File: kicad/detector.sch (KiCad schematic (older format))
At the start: 41 parts, among them J1 Conn_01x05_Male, J2 Conn_01x05_Male, U1 LT1761-5, U2 LT1964-5, U3 REF5010ID, U4 OPA2197xD, U5 OPA2197xD

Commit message: move detector power supplies around (wip)
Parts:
- added H?: MountingHole_Pad, symbol Mechanical:MountingHole_Pad
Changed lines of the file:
@@
 Text Label 10100 1250 0    50   ~ 0
 -Y1
+$Comp
+L Mechanical:MountingHole_Pad H?
+U 1 1 5EA4D075
+P 10100 3450
+F 0 "H?" H 10200 3499 50  0000 L CNN
+F 1 "MountingHole_Pad" H 10200 3408 50  0000 L CNN
+F 2 "" H 10100 3450 50  0001 C CNN
+F 3 "~" H 10100 3450 50  0001 C CNN
+	1    10100 3450
+	1    0    0    -1
+$EndComp
 $EndSCHEMATC

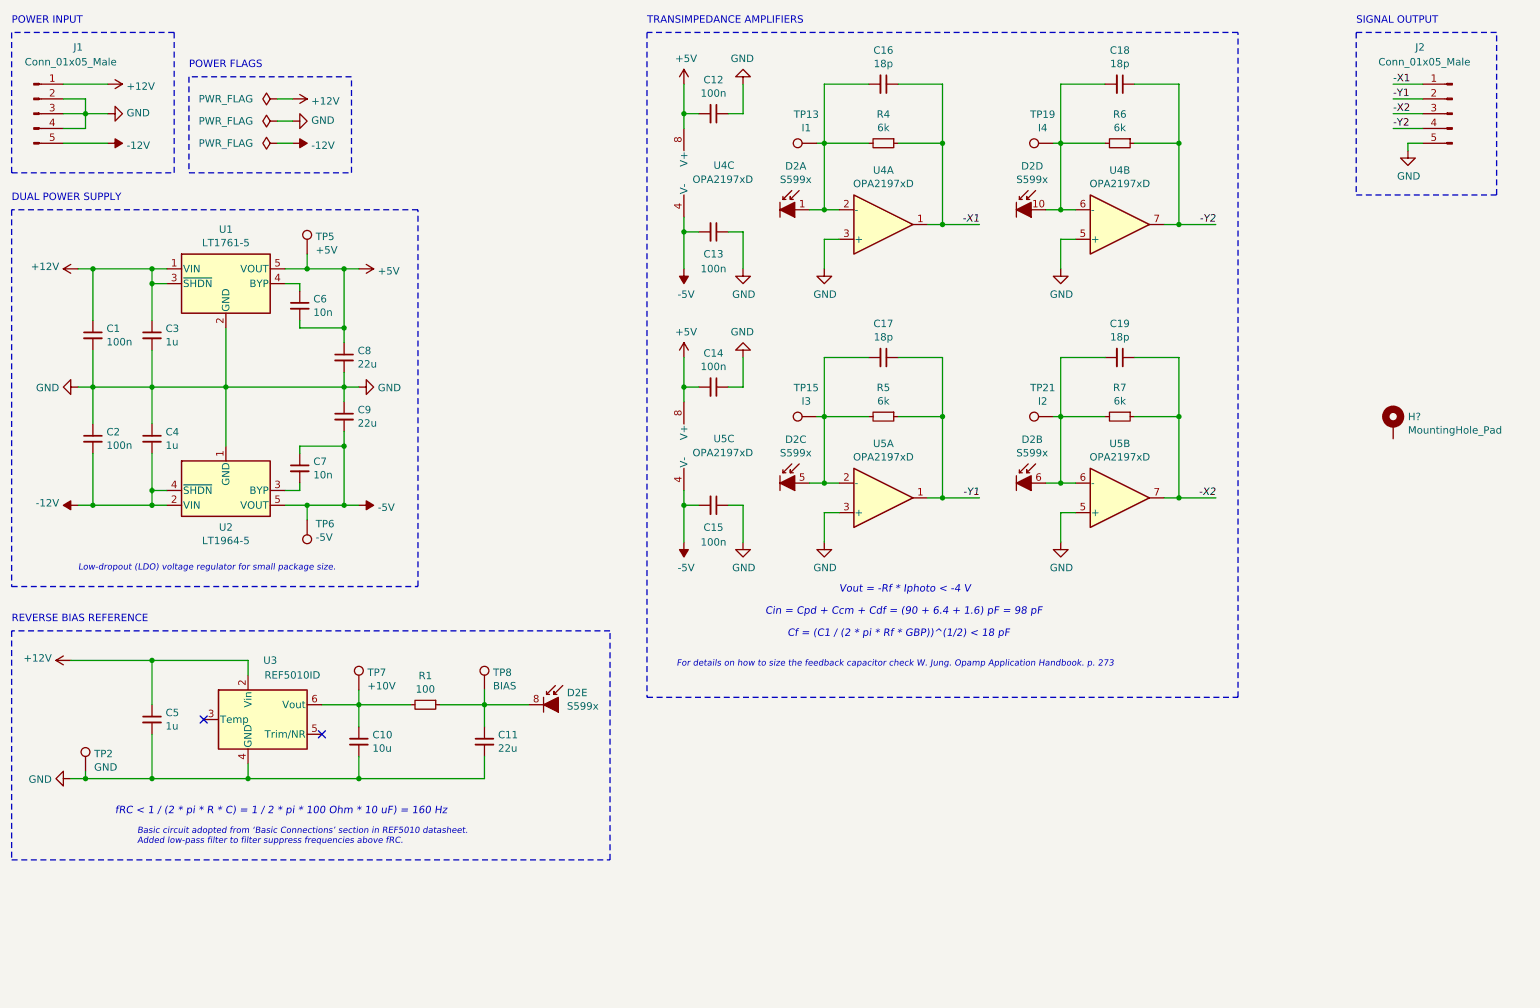
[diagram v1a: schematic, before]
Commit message: added mounting holes to eeschema, replaced mounting holes with pad
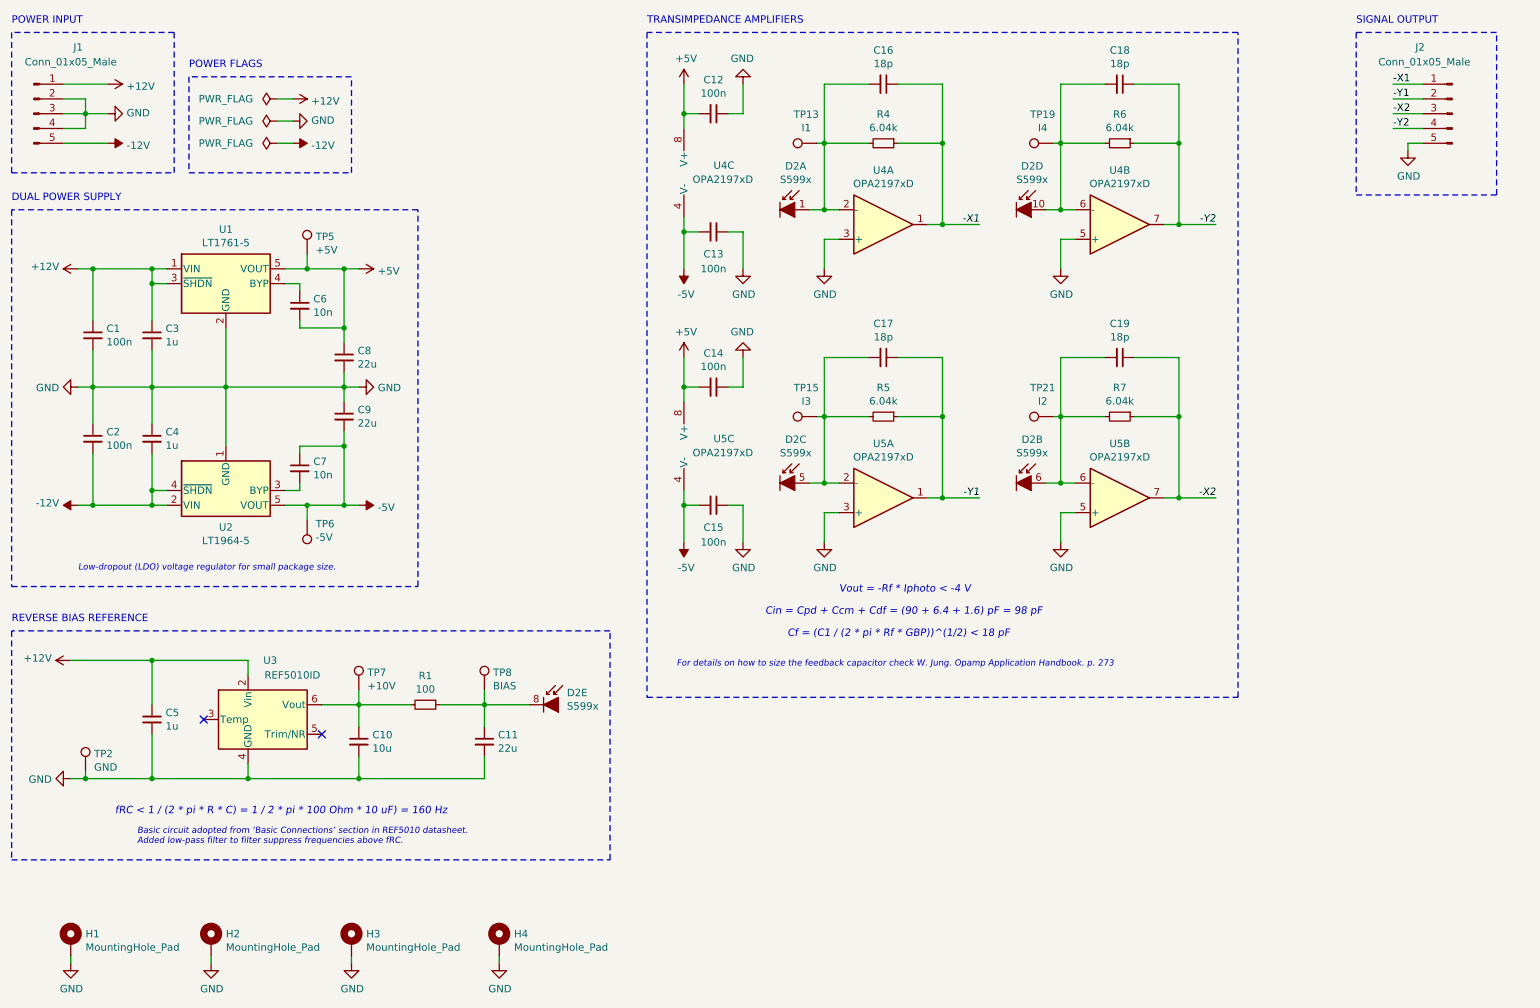
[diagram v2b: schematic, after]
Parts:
- removed H?: MountingHole_Pad, symbol Mechanical:MountingHole_Pad
- added H1, H2, H3, H4: MountingHole_Pad, MountingHole:MountingHole_2.7mm_M2.5_Pad, symbol Mechanical:MountingHole_Pad
- R4, R5, R6, R7: value 6k -> 6.04k
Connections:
- net GND: now also H1.1, H2.1, H3.1, H4.1
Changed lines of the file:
@@
 P 8250 1550
 F 0 "R6" V 8054 1550 50  0000 C CNN
-F 1 "6k" V 8145 1550 50  0000 C CNN
+F 1 "6.04k" V 8145 1550 50  0000 C CNN
 F 2 "Resistor_SMD:R_0603_1608Metric" H 8250 1550 50  0001 C CNN
 F 3 "~" H 8250 1550 50  0001 C CNN
@@
 P 6650 1550
 F 0 "R4" V 6454 1550 50  0000 C CNN
-F 1 "6k" V 6545 1550 50  0000 C CNN
+F 1 "6.04k" V 6545 1550 50  0000 C CNN
 F 2 "Resistor_SMD:R_0603_1608Metric" H 6650 1550 50  0001 C CNN
 F 3 "~" H 6650 1550 50  0001 C CNN
@@
 P 8250 3400
 F 0 "R7" V 8054 3400 50  0000 C CNN
-F 1 "6k" V 8145 3400 50  0000 C CNN
+F 1 "6.04k" V 8145 3400 50  0000 C CNN
 F 2 "Resistor_SMD:R_0603_1608Metric" H 8250 3400 50  0001 C CNN
 F 3 "~" H 8250 3400 50  0001 C CNN
@@
 P 6650 3400
 F 0 "R5" V 6454 3400 50  0000 C CNN
-F 1 "6k" V 6545 3400 50  0000 C CNN
+F 1 "6.04k" V 6545 3400 50  0000 C CNN
 F 2 "Resistor_SMD:R_0603_1608Metric" H 6650 3400 50  0001 C CNN
 F 3 "~" H 6650 3400 50  0001 C CNN
@@
 -Y1
 $Comp
-L Mechanical:MountingHole_Pad H?
-U 1 1 5EA4D075
-P 10100 3450
-F 0 "H?" H 10200 3499 50  0000 L CNN
-F 1 "MountingHole_Pad" H 10200 3408 50  0000 L CNN
-F 2 "" H 10100 3450 50  0001 C CNN
-F 3 "~" H 10100 3450 50  0001 C CNN
-	1    10100 3450
-	1    0    0    -1
-$EndComp
+L Mechanical:MountingHole_Pad H1
+U 1 1 5EA3A96B
+P 1150 6950
+F 0 "H1" H 1250 6999 50  0000 L CNN
+F 1 "MountingHole_Pad" H 1250 6908 50  0000 L CNN
+F 2 "MountingHole:MountingHole_2.7mm_M2.5_Pad" H 1150 6950 50  0001 C CNN
+F 3 "~" H 1150 6950 50  0001 C CNN
+	1    1150 6950
+	1    0    0    -1
+$EndComp
+$Comp
+L Mechanical:MountingHole_Pad H2
+U 1 1 5EA3B177
+P 2100 6950
+F 0 "H2" H 2200 6999 50  0000 L CNN
+F 1 "MountingHole_Pad" H 2200 6908 50  0000 L CNN
+F 2 "MountingHole:MountingHole_2.7mm_M2.5_Pad" H 2100 6950 50  0001 C CNN
+F 3 "~" H 2100 6950 50  0001 C CNN
+	1    2100 6950
+	1    0    0    -1
+$EndComp
+$Comp
+L Mechanical:MountingHole_Pad H3
+U 1 1 5EA3BD34
+P 3050 6950
+F 0 "H3" H 3150 6999 50  0000 L CNN
+F 1 "MountingHole_Pad" H 3150 6908 50  0000 L CNN
+F 2 "MountingHole:MountingHole_2.7mm_M2.5_Pad" H 3050 6950 50  0001 C CNN
+F 3 "~" H 3050 6950 50  0001 C CNN
+	1    3050 6950
+	1    0    0    -1
+$EndComp
+$Comp
+L Mechanical:MountingHole_Pad H4
+U 1 1 5EA3BF9A
+P 4050 6950
+F 0 "H4" H 4150 6999 50  0000 L CNN
+F 1 "MountingHole_Pad" H 4150 6908 50  0000 L CNN
+F 2 "MountingHole:MountingHole_2.7mm_M2.5_Pad" H 4050 6950 50  0001 C CNN
+F 3 "~" H 4050 6950 50  0001 C CNN
+	1    4050 6950
+	1    0    0    -1
+$EndComp
+$Comp
+L power:GND #PWR0115
+U 1 1 5EA3CCB1
+P 1150 7100
+F 0 "#PWR0115" H 1150 6850 50  0001 C CNN
+F 1 "GND" H 1155 6927 50  0000 C CNN
+F 2 "" H 1150 7100 50  0001 C CNN
+F 3 "" H 1150 7100 50  0001 C CNN
+	1    1150 7100
+	1    0    0    -1
+$EndComp
+Wire Wire Line
+	1150 7100 1150 7050
+$Comp
+L power:GND #PWR0116
+U 1 1 5EA46D11
+P 2100 7100
+F 0 "#PWR0116" H 2100 6850 50  0001 C CNN
+F 1 "GND" H 2105 6927 50  0000 C CNN
+F 2 "" H 2100 7100 50  0001 C CNN
+F 3 "" H 2100 7100 50  0001 C CNN
+	1    2100 7100
+	1    0    0    -1
+$EndComp
+Wire Wire Line
+	2100 7100 2100 7050
+$Comp
+L power:GND #PWR0117
+U 1 1 5EA50D8F
+P 3050 7100
+F 0 "#PWR0117" H 3050 6850 50  0001 C CNN
+F 1 "GND" H 3055 6927 50  0000 C CNN
+F 2 "" H 3050 7100 50  0001 C CNN
+F 3 "" H 3050 7100 50  0001 C CNN
+	1    3050 7100
+	1    0    0    -1
+$EndComp
+Wire Wire Line
+	3050 7100 3050 7050
+$Comp
+L power:GND #PWR0118
+U 1 1 5EA64F10
+P 4050 7100
+F 0 "#PWR0118" H 4050 6850 50  0001 C CNN
+F 1 "GND" H 4055 6927 50  0000 C CNN
+F 2 "" H 4050 7100 50  0001 C CNN
+F 3 "" H 4050 7100 50  0001 C CNN
+	1    4050 7100
+	1    0    0    -1
+$EndComp
+Wire Wire Line
+	4050 7100 4050 7050
 $EndSCHEMATC

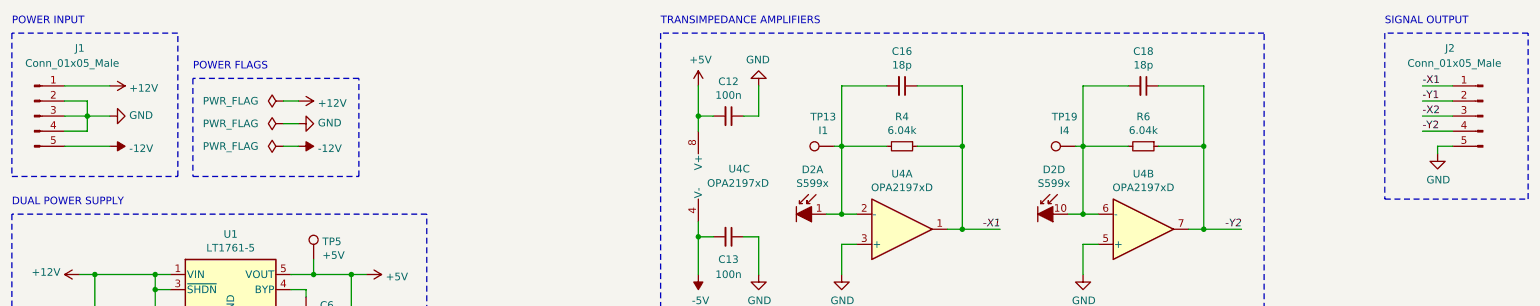
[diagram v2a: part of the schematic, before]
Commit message: changed header shield pins for improved detector routing
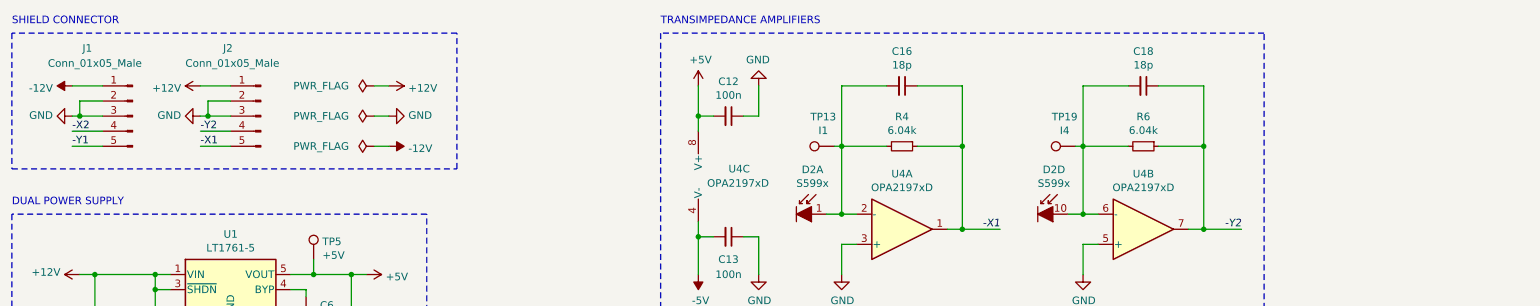
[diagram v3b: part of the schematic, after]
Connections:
- net +12V: now also J2.1 (Pin_1); no longer J1.1 (Pin_1)
- net -12V: now also J1.1 (Pin_1); no longer J1.5 (Pin_5)
- net -X1: now also J2.5 (Pin_5); no longer J2.1 (Pin_1)
- net -X2: now also J1.4 (Pin_4); no longer J2.3 (Pin_3)
- net -Y1: now also J1.5 (Pin_5); no longer J2.2 (Pin_2)
- net GND: now also J2.2 (Pin_2), J2.3 (Pin_3); no longer J1.4 (Pin_4), J2.5 (Pin_5)
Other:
- note added: "SHIELD CONNECTOR"
- note removed: "POWER FLAGS"
- note removed: "POWER INPUT"
- note removed: "SIGNAL OUTPUT"
- moved on the sheet: J1, J2
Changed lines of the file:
@@
 	1    0    0    1
 $EndComp
-Text Label 10100 1150 0    50   ~ 0
+Text Label 2000 1550 0    50   ~ 0
 -X1
-Wire Wire Line
-	10100 1150 10300 1150
-Text Label 10100 1350 0    50   ~ 0
+Text Label 1150 1450 0    50   ~ 0
 -X2
 Wire Wire Line
-	10100 1250 10300 1250
-Wire Wire Line
-	10100 1350 10300 1350
-Wire Wire Line
-	10100 1450 10300 1450
-Wire Notes Line
-	750  800  750  1750
-Wire Notes Line
-	1850 1750 1850 800
-Wire Notes Line
-	1850 800  750  800
-Text Notes 750  750  0    50   ~ 0
-POWER INPUT
-Wire Notes Line
-	9850 1900 10800 1900
-Wire Notes Line
-	10800 1900 10800 800
-Wire Notes Line
-	10800 800  9850 800
-Wire Notes Line
-	9850 800  9850 1900
-Text Notes 9850 750  0    50   ~ 0
-SIGNAL OUTPUT
+	2050 1250 2200 1250
+Wire Wire Line
+	2050 1350 2200 1350
+Wire Wire Line
+	2000 1450 2200 1450
 Wire Wire Line
 	6250 2200 6250 2400
@@
 L power:PWR_FLAG #FLG0103
 U 1 1 5E844871
-P 2550 1250
-F 0 "#FLG0103" H 2550 1325 50  0001 C CNN
-F 1 "PWR_FLAG" V 2550 1600 50  0000 C CNN
-F 2 "" H 2550 1250 50  0001 C CNN
-F 3 "~" H 2550 1250 50  0001 C CNN
-	1    2550 1250
+P 3150 1150
+F 0 "#FLG0103" H 3150 1225 50  0001 C CNN
+F 1 "PWR_FLAG" V 3150 1500 50  0000 C CNN
+F 2 "" H 3150 1150 50  0001 C CNN
+F 3 "~" H 3150 1150 50  0001 C CNN
+	1    3150 1150
 	0    -1   1    0
 $EndComp
@@
 L power:+12V #PWR0101
 U 1 1 5EB34081
-P 2650 1250
-F 0 "#PWR0101" H 2650 1100 50  0001 C CNN
-F 1 "+12V" V 2665 1378 50  0000 L CNN
-F 2 "" H 2650 1250 50  0001 C CNN
-F 3 "" H 2650 1250 50  0001 C CNN
-	1    2650 1250
+P 3250 1150
+F 0 "#PWR0101" H 3250 1000 50  0001 C CNN
+F 1 "+12V" V 3265 1278 50  0000 L CNN
+F 2 "" H 3250 1150 50  0001 C CNN
+F 3 "" H 3250 1150 50  0001 C CNN
+	1    3250 1150
 	0    1    1    0
 $EndComp
@@
 L power:GND #PWR0102
 U 1 1 5EB6A7CA
-P 2650 1400
-F 0 "#PWR0102" H 2650 1150 50  0001 C CNN
-F 1 "GND" V 2655 1272 50  0000 R CNN
-F 2 "" H 2650 1400 50  0001 C CNN
-F 3 "" H 2650 1400 50  0001 C CNN
-	1    2650 1400
+P 3250 1350
+F 0 "#PWR0102" H 3250 1100 50  0001 C CNN
+F 1 "GND" V 3255 1222 50  0000 R CNN
+F 2 "" H 3250 1350 50  0001 C CNN
+F 3 "" H 3250 1350 50  0001 C CNN
+	1    3250 1350
 	0    -1   -1   0
 $EndComp
@@
 L power:-12V #PWR0108
 U 1 1 5EB9E634
-P 2650 1550
-F 0 "#PWR0108" H 2650 1650 50  0001 C CNN
-F 1 "-12V" V 2665 1678 50  0000 L CNN
-F 2 "" H 2650 1550 50  0001 C CNN
-F 3 "" H 2650 1550 50  0001 C CNN
-	1    2650 1550
+P 3250 1550
+F 0 "#PWR0108" H 3250 1650 50  0001 C CNN
+F 1 "-12V" V 3265 1678 50  0000 L CNN
+F 2 "" H 3250 1550 50  0001 C CNN
+F 3 "" H 3250 1550 50  0001 C CNN
+	1    3250 1550
 	0    1    1    0
 $EndComp
 Wire Wire Line
-	2550 1250 2650 1250
-$Comp
-L power:PWR_FLAG #FLG0101
-U 1 1 5EC59A7B
-P 2550 1400
-F 0 "#FLG0101" H 2550 1475 50  0001 C CNN
-F 1 "PWR_FLAG" V 2550 1750 50  0000 C CNN
-F 2 "" H 2550 1400 50  0001 C CNN
-F 3 "~" H 2550 1400 50  0001 C CNN
-	1    2550 1400
-	0    -1   1    0
-$EndComp
-Wire Wire Line
-	2550 1400 2650 1400
+	3150 1150 3250 1150
+Wire Wire Line
+	3150 1350 3250 1350
 $Comp
 L power:PWR_FLAG #FLG0102
 U 1 1 5EC64D0D
-P 2550 1550
-F 0 "#FLG0102" H 2550 1625 50  0001 C CNN
-F 1 "PWR_FLAG" V 2550 1900 50  0000 C CNN
-F 2 "" H 2550 1550 50  0001 C CNN
-F 3 "~" H 2550 1550 50  0001 C CNN
-	1    2550 1550
-	0    -1   1    0
-$EndComp
-Wire Wire Line
-	2550 1550 2650 1550
-Wire Wire Line
-	1250 1350 1400 1350
-Wire Wire Line
-	1100 1150 1400 1150
-Wire Wire Line
-	1100 1550 1400 1550
-Wire Wire Line
-	1250 1250 1100 1250
-Wire Wire Line
-	1250 1350 1250 1250
-Connection ~ 1250 1350
-Wire Wire Line
-	1250 1450 1250 1350
-Wire Wire Line
-	1100 1450 1250 1450
-$Comp
-L power:+12V #PWR0109
-U 1 1 5E9CD504
-P 1400 1150
-F 0 "#PWR0109" H 1400 1000 50  0001 C CNN
-F 1 "+12V" V 1415 1278 50  0000 L CNN
-F 2 "" H 1400 1150 50  0001 C CNN
-F 3 "" H 1400 1150 50  0001 C CNN
-	1    1400 1150
-	0    1    1    0
-$EndComp
+P 3150 1550
+F 0 "#FLG0102" H 3150 1625 50  0001 C CNN
+F 1 "PWR_FLAG" V 3150 1900 50  0000 C CNN
+F 2 "" H 3150 1550 50  0001 C CNN
+F 3 "~" H 3150 1550 50  0001 C CNN
+	1    3150 1550
+	0    -1   1    0
+$EndComp
+Wire Wire Line
+	3150 1550 3250 1550
+Wire Wire Line
+	1200 1350 1150 1350
+Wire Wire Line
+	1350 1150 1150 1150
+Wire Wire Line
+	1350 1550 1150 1550
+Wire Wire Line
+	1200 1250 1350 1250
+Wire Wire Line
+	1200 1350 1200 1250
+Connection ~ 1200 1350
 $Comp
 L power:-12V #PWR0110
 U 1 1 5E9CDF97
-P 1400 1550
-F 0 "#PWR0110" H 1400 1650 50  0001 C CNN
-F 1 "-12V" V 1415 1678 50  0000 L CNN
-F 2 "" H 1400 1550 50  0001 C CNN
-F 3 "" H 1400 1550 50  0001 C CNN
-	1    1400 1550
-	0    1    1    0
+P 1150 1150
+F 0 "#PWR0110" H 1150 1250 50  0001 C CNN
+F 1 "-12V" V 1165 1278 50  0000 L CNN
+F 2 "" H 1150 1150 50  0001 C CNN
+F 3 "" H 1150 1150 50  0001 C CNN
+	1    1150 1150
+	0    -1   1    0
 $EndComp
 $Comp
 L power:GND #PWR0111
 U 1 1 5E9D8FA6
-P 1400 1350
-F 0 "#PWR0111" H 1400 1100 50  0001 C CNN
-F 1 "GND" V 1405 1222 50  0000 R CNN
-F 2 "" H 1400 1350 50  0001 C CNN
-F 3 "" H 1400 1350 50  0001 C CNN
-	1    1400 1350
-	0    -1   -1   0
-$EndComp
-Wire Wire Line
-	1100 1350 1250 1350
+P 1150 1350
+F 0 "#PWR0111" H 1150 1100 50  0001 C CNN
+F 1 "GND" V 1155 1222 50  0000 R CNN
+F 2 "" H 1150 1350 50  0001 C CNN
+F 3 "" H 1150 1350 50  0001 C CNN
+	1    1150 1350
+	0    1    -1   0
+$EndComp
+Wire Wire Line
+	1350 1350 1200 1350
 $Comp
 L Connector:Conn_01x05_Male J1
 U 1 1 5E9B51ED
-P 900 1350
-F 0 "J1" H 1200 1800 50  0000 C CNN
-F 1 "Conn_01x05_Male" H 1150 1700 50  0000 C CNN
-F 2 "Connector_PinSocket_2.54mm:PinSocket_1x05_P2.54mm_Vertical" H 900 1350 50  0001 C CNN
-F 3 "~" H 900 1350 50  0001 C CNN
-	1    900  1350
-	1    0    0    -1
-$EndComp
-Wire Notes Line
-	750  1750 1850 1750
-Wire Notes Line
-	1950 1100 1950 1750
-Wire Notes Line
-	1950 1750 3050 1750
-Wire Notes Line
-	3050 1750 3050 1100
-Wire Notes Line
-	3050 1100 1950 1100
-Text Notes 1950 1050 0    50   ~ 0
-POWER FLAGS
-$Comp
-L Connector:Conn_01x05_Male J2
-U 1 1 5EDB6E60
-P 10500 1350
-F 0 "J2" H 10750 1800 50  0000 R CNN
-F 1 "Conn_01x05_Male" H 11000 1700 50  0000 R CNN
-F 2 "Connector_PinSocket_2.54mm:PinSocket_1x05_P2.54mm_Vertical" H 10500 1350 50  0001 C CNN
-F 3 "~" H 10500 1350 50  0001 C CNN
-	1    10500 1350
+P 1550 1350
+F 0 "J1" H 1850 1800 50  0000 C CNN
+F 1 "Conn_01x05_Male" H 1800 1700 50  0000 C CNN
+F 2 "Connector_PinSocket_2.54mm:PinSocket_1x05_P2.54mm_Vertical" H 1550 1350 50  0001 C CNN
+F 3 "~" H 1550 1350 50  0001 C CNN
+	1    1550 1350
 	-1   0    0    -1
 $EndComp
-$Comp
-L power:GND #PWR0112
-U 1 1 5EDBA180
-P 10200 1600
-F 0 "#PWR0112" H 10200 1350 50  0001 C CNN
-F 1 "GND" H 10205 1427 50  0000 C CNN
-F 2 "" H 10200 1600 50  0001 C CNN
-F 3 "" H 10200 1600 50  0001 C CNN
-	1    10200 1600
-	1    0    0    -1
-$EndComp
-Wire Wire Line
-	10200 1600 10200 1550
-Wire Wire Line
-	10200 1550 10300 1550
+Wire Wire Line
+	2000 1550 2200 1550
 $Comp
 L power:+12V #PWR0103
@@
 Wire Wire Line
 	1300 4000 1700 4000
-Text Label 10100 1450 0    50   ~ 0
+Text Label 2000 1450 0    50   ~ 0
 -Y2
-Text Label 10100 1250 0    50   ~ 0
+Text Label 1150 1550 0    50   ~ 0
 -Y1
 $Comp
@@
 Wire Wire Line
 	4050 7100 4050 7050
+Wire Wire Line
+	2050 1350 2050 1250
+Connection ~ 2050 1350
+Wire Wire Line
+	1150 1450 1350 1450
+$Comp
+L Connector:Conn_01x05_Male J2
+U 1 1 5EDB6E60
+P 2400 1350
+F 0 "J2" H 2650 1800 50  0000 R CNN
+F 1 "Conn_01x05_Male" H 2900 1700 50  0000 R CNN
+F 2 "Connector_PinSocket_2.54mm:PinSocket_1x05_P2.54mm_Vertical" H 2400 1350 50  0001 C CNN
+F 3 "~" H 2400 1350 50  0001 C CNN
+	1    2400 1350
+	-1   0    0    -1
+$EndComp
+$Comp
+L power:PWR_FLAG #FLG0101
+U 1 1 5EC59A7B
+P 3150 1350
+F 0 "#FLG0101" H 3150 1425 50  0001 C CNN
+F 1 "PWR_FLAG" V 3150 1700 50  0000 C CNN
+F 2 "" H 3150 1350 50  0001 C CNN
+F 3 "~" H 3150 1350 50  0001 C CNN
+	1    3150 1350
+	0    -1   1    0
+$EndComp
+Wire Wire Line
+	2050 1350 2000 1350
+$Comp
+L power:GND #PWR0112
+U 1 1 5ED37047
+P 2000 1350
+F 0 "#PWR0112" H 2000 1100 50  0001 C CNN
+F 1 "GND" V 2005 1222 50  0000 R CNN
+F 2 "" H 2000 1350 50  0001 C CNN
+F 3 "" H 2000 1350 50  0001 C CNN
+	1    2000 1350
+	0    1    -1   0
+$EndComp
+Wire Wire Line
+	2000 1150 2200 1150
+$Comp
+L power:+12V #PWR0109
+U 1 1 5E9CD504
+P 2000 1150
+F 0 "#PWR0109" H 2000 1000 50  0001 C CNN
+F 1 "+12V" V 2015 1278 50  0000 L CNN
+F 2 "" H 2000 1150 50  0001 C CNN
+F 3 "" H 2000 1150 50  0001 C CNN
+	1    2000 1150
+	0    -1   1    0
+$EndComp
+Wire Notes Line
+	750  800  750  1700
+Wire Notes Line
+	750  1700 3700 1700
+Wire Notes Line
+	3700 1700 3700 800
+Wire Notes Line
+	3700 800  750  800
+Text Notes 750  750  0    50   ~ 0
+SHIELD CONNECTOR
 $EndSCHEMATC
